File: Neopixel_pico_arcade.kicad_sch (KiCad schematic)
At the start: 10 parts

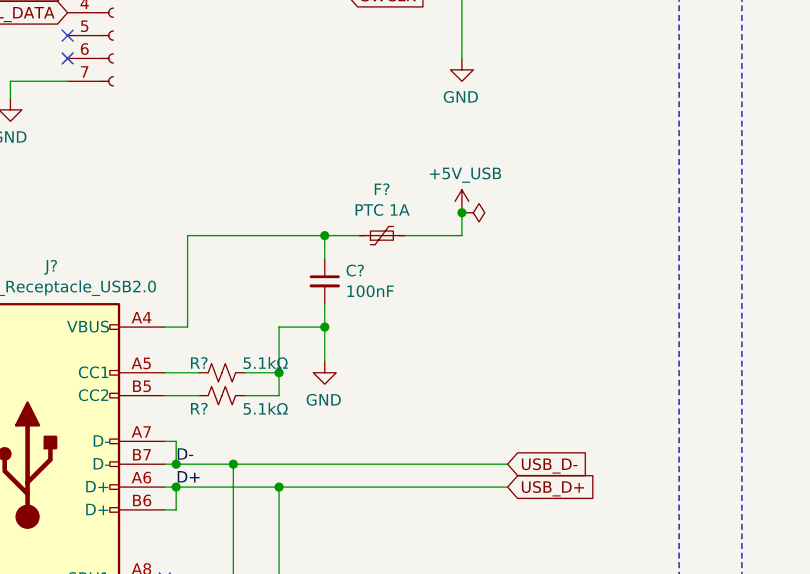
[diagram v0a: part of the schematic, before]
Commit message: Adds bulk capacitance for USB power
USB devices should be limited to at most 10µF capacitance to keep inrush
current under the specified limits.
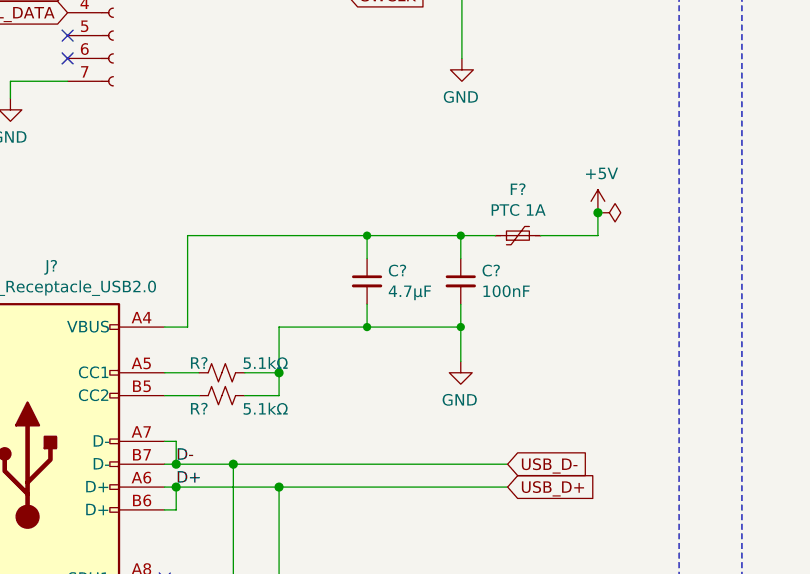
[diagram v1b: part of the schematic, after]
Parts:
- added C?: 4.7µF, Capacitor_SMD:C_0805_2012Metric_Pad1.18x1.45mm_HandSolder, symbol Device:C_Small
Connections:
- net GND: now also C?.2
- net at C?.1, F?.1, J?.A4 (VBUS)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: now also C?.1
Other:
- moved on the sheet: C?, F?
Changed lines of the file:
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@@
   (junction (at 69.215 90.17) (diameter 1.016) (color 0 0 0 0))
   (junction (at 69.215 102.87) (diameter 1.016) (color 0 0 0 0))
-  (junction (at 74.295 74.93) (diameter 1.016) (color 0 0 0 0))
-  (junction (at 74.295 85.09) (diameter 1.016) (color 0 0 0 0))
-  (junction (at 89.535 72.39) (diameter 1.016) (color 0 0 0 0))
+  (junction (at 78.994 74.93) (diameter 0) (color 0 0 0 0))
+  (junction (at 78.994 85.09) (diameter 0) (color 0 0 0 0))
+  (junction (at 89.408 74.93) (diameter 0) (color 0 0 0 0))
+  (junction (at 89.408 85.09) (diameter 0) (color 0 0 0 0))
+  (junction (at 104.648 72.39) (diameter 1.016) (color 0 0 0 0))
   (no_connect (at 45.72 52.705))
   (no_connect (at 45.72 55.245))
@@
     (stroke (width 0) (type solid) (color 0 0 0 0))
   )
-  (wire (pts (xy 59.055 74.93) (xy 74.295 74.93))
-    (stroke (width 0) (type solid) (color 0 0 0 0))
+  (wire (pts (xy 59.055 74.93) (xy 78.994 74.93))
+    (stroke (width 0) (type default) (color 0 0 0 0))
   )
   (wire (pts (xy 64.135 100.33) (xy 64.135 121.92))
@@
     (stroke (width 0) (type solid) (color 0 0 0 0))
   )
-  (wire (pts (xy 69.215 85.09) (xy 74.295 85.09))
+  (wire (pts (xy 69.215 85.09) (xy 78.994 85.09))
     (stroke (width 0) (type solid) (color 0 0 0 0))
   )
@@
     (stroke (width 0) (type solid) (color 0 0 0 0))
   )
-  (wire (pts (xy 74.295 74.93) (xy 74.295 77.47))
-    (stroke (width 0) (type solid) (color 0 0 0 0))
-  )
-  (wire (pts (xy 74.295 74.93) (xy 78.105 74.93))
-    (stroke (width 0) (type solid) (color 0 0 0 0))
-  )
-  (wire (pts (xy 74.295 82.55) (xy 74.295 85.09))
-    (stroke (width 0) (type solid) (color 0 0 0 0))
-  )
-  (wire (pts (xy 74.295 85.09) (xy 74.295 88.9))
-    (stroke (width 0) (type solid) (color 0 0 0 0))
-  )
   (wire (pts (xy 76.835 45.72) (xy 89.535 45.72))
     (stroke (width 0) (type solid) (color 0 0 0 0))
@@
     (stroke (width 0) (type solid) (color 0 0 0 0))
   )
+  (wire (pts (xy 78.994 74.93) (xy 78.994 77.47))
+    (stroke (width 0) (type default) (color 0 0 0 0))
+  )
+  (wire (pts (xy 78.994 74.93) (xy 89.408 74.93))
+    (stroke (width 0) (type default) (color 0 0 0 0))
+  )
+  (wire (pts (xy 78.994 82.55) (xy 78.994 85.09))
+    (stroke (width 0) (type default) (color 0 0 0 0))
+  )
+  (wire (pts (xy 78.994 85.09) (xy 89.408 85.09))
+    (stroke (width 0) (type solid) (color 0 0 0 0))
+  )
   (wire (pts (xy 79.375 134.62) (xy 83.185 134.62))
     (stroke (width 0) (type solid) (color 0 0 0 0))
   )
-  (wire (pts (xy 83.185 74.93) (xy 89.535 74.93))
-    (stroke (width 0) (type solid) (color 0 0 0 0))
-  )
   (wire (pts (xy 83.185 133.35) (xy 83.185 134.62))
     (stroke (width 0) (type solid) (color 0 0 0 0))
   )
+  (wire (pts (xy 89.408 74.93) (xy 89.408 77.47))
+    (stroke (width 0) (type solid) (color 0 0 0 0))
+  )
+  (wire (pts (xy 89.408 74.93) (xy 93.218 74.93))
+    (stroke (width 0) (type solid) (color 0 0 0 0))
+  )
+  (wire (pts (xy 89.408 82.55) (xy 89.408 85.09))
+    (stroke (width 0) (type solid) (color 0 0 0 0))
+  )
+  (wire (pts (xy 89.408 85.09) (xy 89.408 88.9))
+    (stroke (width 0) (type solid) (color 0 0 0 0))
+  )
   (wire (pts (xy 89.535 45.72) (xy 89.535 55.245))
     (stroke (width 0) (type solid) (color 0 0 0 0))
   )
-  (wire (pts (xy 89.535 74.93) (xy 89.535 72.39))
+  (wire (pts (xy 98.298 74.93) (xy 104.648 74.93))
+    (stroke (width 0) (type solid) (color 0 0 0 0))
+  )
+  (wire (pts (xy 104.648 74.93) (xy 104.648 72.39))
     (stroke (width 0) (type solid) (color 0 0 0 0))
   )
@@
     (pin "1")
   )
-  (symbol (lib_id "Generative_picture:+5V_USB") (at 89.535 72.39 0) (unit 1)
-    (in_bom yes) (on_board yes)
-    (property "Reference" "#PWR?" (id 0) (at 89.535 76.2 0)
-      (effects (font (size 1.27 1.27)) hide)
-    )
-    (property "Value" "+5V_USB" (id 1) (at 89.9033 68.0656 0))
-    (property "Footprint" "" (id 2) (at 89.535 72.39 0)
-      (effects (font (size 1.27 1.27)) hide)
-    )
-    (property "Datasheet" "" (id 3) (at 89.535 72.39 0)
+  (symbol (lib_id "Generative_picture:+5V_USB") (at 104.648 72.39 0) (unit 1)
+    (in_bom yes) (on_board yes)
+    (property "Reference" "#PWR?" (id 0) (at 104.648 76.2 0)
+      (effects (font (size 1.27 1.27)) hide)
+    )
+    (property "Value" "+5V" (id 1) (at 105.0163 68.0656 0))
+    (property "Footprint" "" (id 2) (at 104.648 72.39 0)
+      (effects (font (size 1.27 1.27)) hide)
+    )
+    (property "Datasheet" "" (id 3) (at 104.648 72.39 0)
       (effects (font (size 1.27 1.27)) hide)
     )
@@
     (pin "1")
   )
-  (symbol (lib_id "power:PWR_FLAG") (at 89.535 72.39 270) (unit 1)
-    (in_bom yes) (on_board yes)
-    (property "Reference" "#FLG?" (id 0) (at 91.44 72.39 0)
-      (effects (font (size 1.27 1.27)) hide)
-    )
-    (property "Value" "PWR_FLAG" (id 1) (at 92.71 72.39 90)
+  (symbol (lib_id "power:PWR_FLAG") (at 104.648 72.39 270) (unit 1)
+    (in_bom yes) (on_board yes)
+    (property "Reference" "#FLG?" (id 0) (at 106.553 72.39 0)
+      (effects (font (size 1.27 1.27)) hide)
+    )
+    (property "Value" "PWR_FLAG" (id 1) (at 107.823 72.39 90)
       (effects (font (size 1.27 1.27)) (justify left) hide)
     )
-    (property "Footprint" "" (id 2) (at 89.535 72.39 0)
-      (effects (font (size 1.27 1.27)) hide)
-    )
-    (property "Datasheet" "~" (id 3) (at 89.535 72.39 0)
+    (property "Footprint" "" (id 2) (at 104.648 72.39 0)
+      (effects (font (size 1.27 1.27)) hide)
+    )
+    (property "Datasheet" "~" (id 3) (at 104.648 72.39 0)
       (effects (font (size 1.27 1.27)) hide)
     )
@@
     (pin "1")
   )
-  (symbol (lib_id "power:GND") (at 74.295 88.9 0) (mirror y) (unit 1)
-    (in_bom yes) (on_board yes)
-    (property "Reference" "#PWR?" (id 0) (at 74.295 95.25 0)
-      (effects (font (size 1.27 1.27)) hide)
-    )
-    (property "Value" "GND" (id 1) (at 74.1807 93.2244 0))
-    (property "Footprint" "" (id 2) (at 74.295 88.9 0)
-      (effects (font (size 1.27 1.27)) hide)
-    )
-    (property "Datasheet" "" (id 3) (at 74.295 88.9 0)
+  (symbol (lib_id "power:GND") (at 89.408 88.9 0) (mirror y) (unit 1)
+    (in_bom yes) (on_board yes)
+    (property "Reference" "#PWR?" (id 0) (at 89.408 95.25 0)
+      (effects (font (size 1.27 1.27)) hide)
+    )
+    (property "Value" "GND" (id 1) (at 89.2937 93.2244 0))
+    (property "Footprint" "" (id 2) (at 89.408 88.9 0)
+      (effects (font (size 1.27 1.27)) hide)
+    )
+    (property "Datasheet" "" (id 3) (at 89.408 88.9 0)
       (effects (font (size 1.27 1.27)) hide)
     )
@@
     (pin "2")
   )
-  (symbol (lib_id "Device:Polyfuse_Small") (at 80.645 74.93 90) (unit 1)
-    (in_bom yes) (on_board yes)
-    (property "Reference" "F?" (id 0) (at 80.645 69.8308 90))
-    (property "Value" "PTC 1A" (id 1) (at 80.645 72.13 90))
-    (property "Footprint" "Generative_picture:Belfuse_0ZCJ" (id 2) (at 85.725 73.66 0)
+  (symbol (lib_id "Device:Polyfuse_Small") (at 95.758 74.93 90) (unit 1)
+    (in_bom yes) (on_board yes)
+    (property "Reference" "F?" (id 0) (at 95.758 69.8308 90))
+    (property "Value" "PTC 1A" (id 1) (at 95.758 72.13 90))
+    (property "Footprint" "Generative_picture:Belfuse_0ZCJ" (id 2) (at 100.838 73.66 0)
       (effects (font (size 1.27 1.27)) (justify left) hide)
     )
-    (property "Datasheet" "~" (id 3) (at 80.645 74.93 0)
+    (property "Datasheet" "~" (id 3) (at 95.758 74.93 0)
       (effects (font (size 1.27 1.27)) hide)
     )
@@
     (pin "2")
   )
-  (symbol (lib_id "Device:C_Small") (at 74.295 80.01 0) (unit 1)
-    (in_bom yes) (on_board yes)
-    (property "Reference" "C?" (id 0) (at 76.6192 78.8606 0)
+  (symbol (lib_id "Device:C_Small") (at 78.994 80.01 0) (unit 1)
+    (in_bom yes) (on_board yes)
+    (property "Reference" "C?" (id 0) (at 81.3182 78.8606 0)
       (effects (font (size 1.27 1.27)) (justify left))
     )
-    (property "Value" "100nF" (id 1) (at 76.619 81.159 0)
+    (property "Value" "4.7µF" (id 1) (at 81.318 81.159 0)
       (effects (font (size 1.27 1.27)) (justify left))
     )
-    (property "Footprint" "Capacitor_SMD:C_0805_2012Metric_Pad1.18x1.45mm_HandSolder" (id 2) (at 74.295 80.01 0)
-      (effects (font (size 1.27 1.27)) hide)
-    )
-    (property "Datasheet" "~" (id 3) (at 74.295 80.01 0)
+    (property "Footprint" "Capacitor_SMD:C_0805_2012Metric_Pad1.18x1.45mm_HandSolder" (id 2) (at 78.994 80.01 0)
+      (effects (font (size 1.27 1.27)) hide)
+    )
+    (property "Datasheet" "~" (id 3) (at 78.994 80.01 0)
+      (effects (font (size 1.27 1.27)) hide)
+    )
+    (pin "1")
+    (pin "2")
+  )
+  (symbol (lib_id "Device:C_Small") (at 89.408 80.01 0) (unit 1)
+    (in_bom yes) (on_board yes)
+    (property "Reference" "C?" (id 0) (at 91.7322 78.8606 0)
+      (effects (font (size 1.27 1.27)) (justify left))
+    )
+    (property "Value" "100nF" (id 1) (at 91.732 81.159 0)
+      (effects (font (size 1.27 1.27)) (justify left))
+    )
+    (property "Footprint" "Capacitor_SMD:C_0805_2012Metric_Pad1.18x1.45mm_HandSolder" (id 2) (at 89.408 80.01 0)
+      (effects (font (size 1.27 1.27)) hide)
+    )
+    (property "Datasheet" "~" (id 3) (at 89.408 80.01 0)
       (effects (font (size 1.27 1.27)) hide)
     )
@@
     )
     (path "/4f1fe51c-79e1-410a-ae57-948c663e40fc"
-      (reference "#PWR?") (unit 1) (value "+5V_USB") (footprint "")
+      (reference "#PWR?") (unit 1) (value "+5V") (footprint "")
     )
     (path "/ed4fcb8f-53b7-458f-bfaa-4aa127051293/5012d051-6b17-499c-a0aa-a1866e5f78d5"
@@
       (reference "C?") (unit 1) (value "100nF") (footprint "Capacitor_SMD:C_0805_2012Metric_Pad1.15x1.40mm_HandSolder")
     )
+    (path "/3dcd957e-2bc0-456f-b0ec-92b7bc5b3d89"
+      (reference "C?") (unit 1) (value "4.7µF") (footprint "Capacitor_SMD:C_0805_2012Metric_Pad1.18x1.45mm_HandSolder")
+    )
     (path "/ed4fcb8f-53b7-458f-bfaa-4aa127051293/45a55838-3e5c-4754-93c1-b22db5fcfdfc"

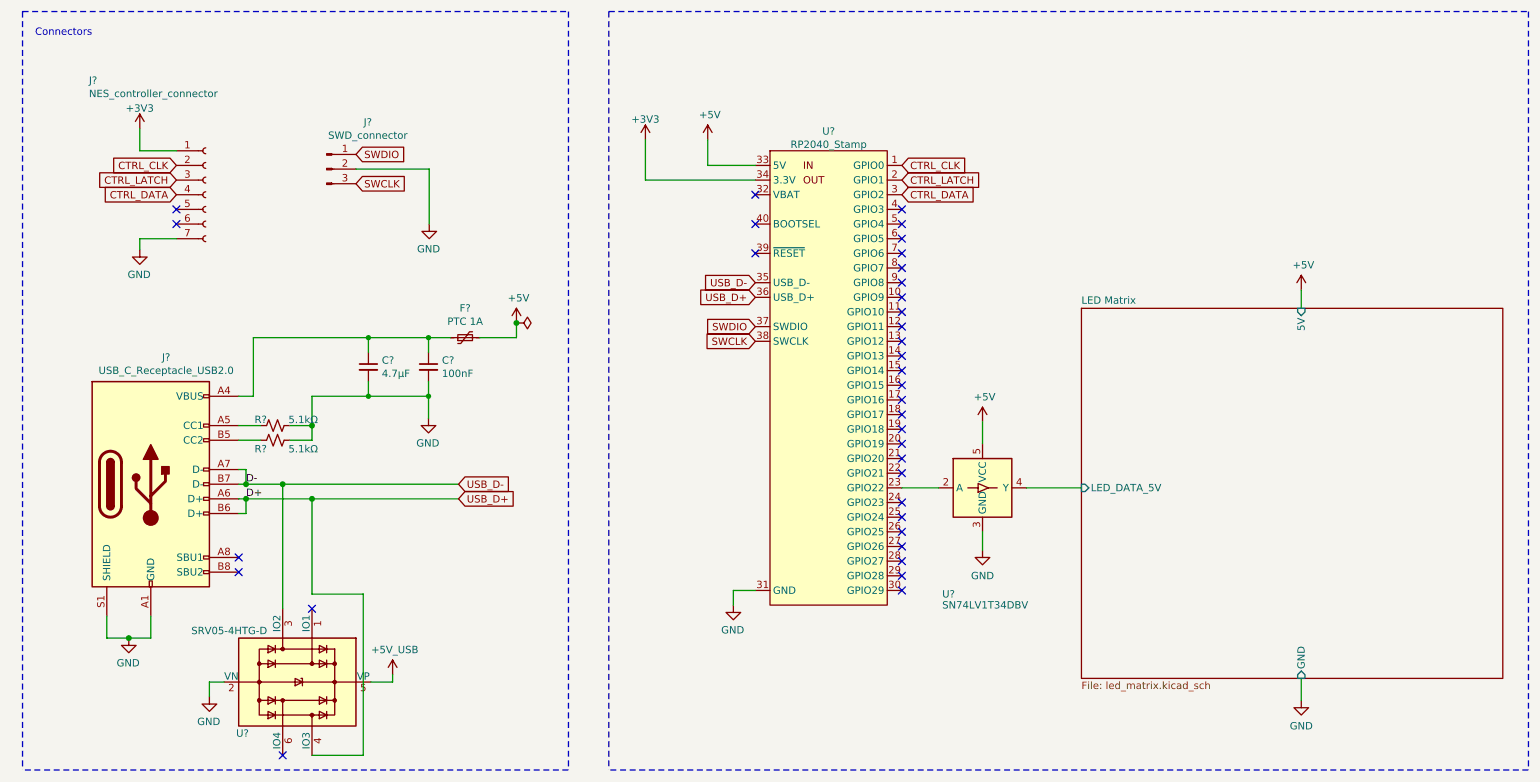
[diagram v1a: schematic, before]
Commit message: Adds jumpers to latch and clock lines to make rework easier
I've switched those two pins a few times already during prototyping.
With the normally closed jumpers it will be easier to swap them if I
make a mistake while laying out the board.
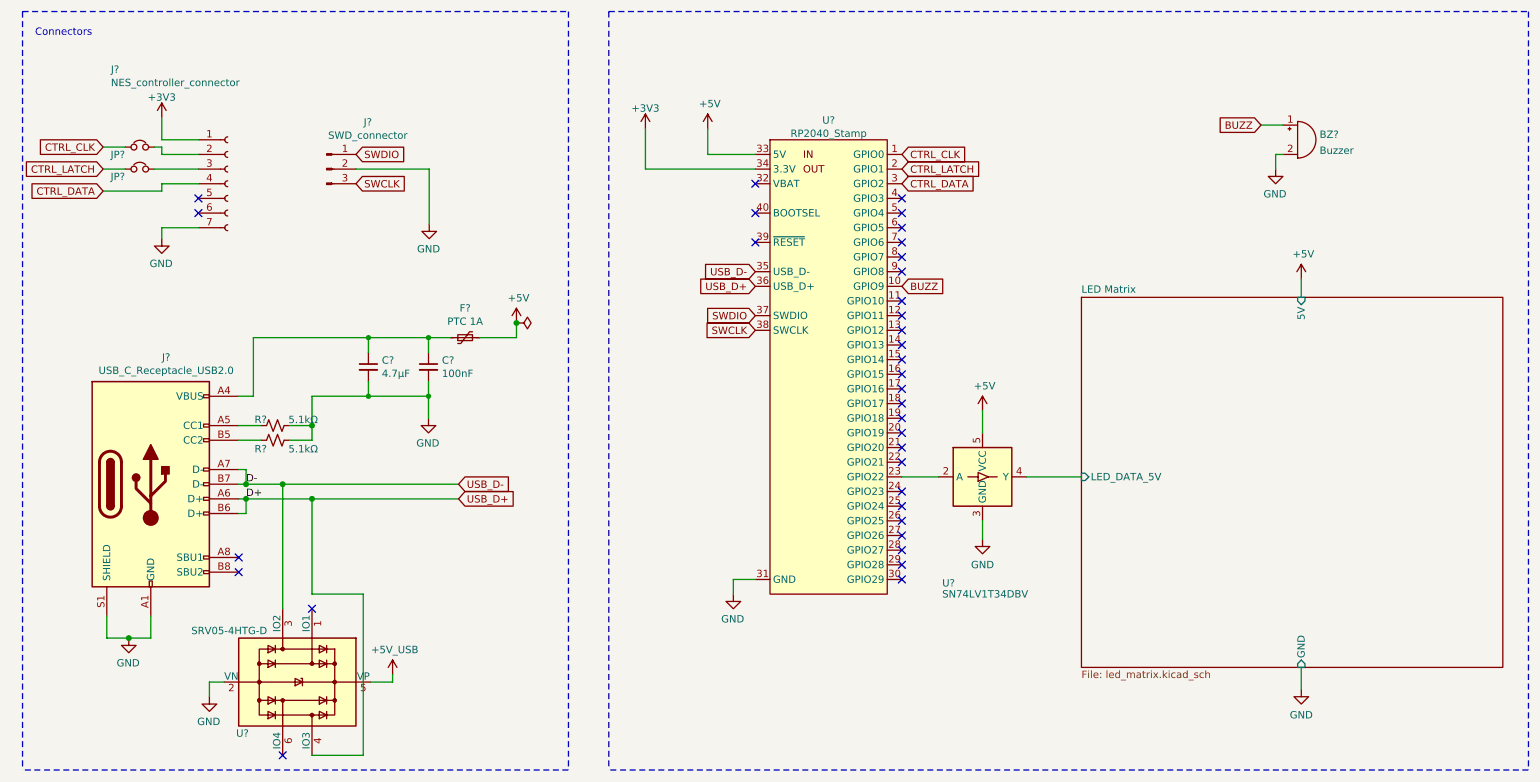
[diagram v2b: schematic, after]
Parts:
- added BZ?: Buzzer, symbol Device:Buzzer
- added JP? (x2): jmp, symbol Device:Jumper_NC_Small
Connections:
- net CTRL_CLK: now also JP?.1; no longer J?.2 (Pin_2)
- net CTRL_LATCH: now also JP?.1; no longer J?.3 (Pin_3)
- net GND: now also BZ?.2 (+)
- net BUZZ: now reaches U?.10 (GPIO9)
- net BUZZ: now also BZ?.1 (-)
- new net: J?.2 (Pin_2), JP?.2
- new net: J?.3 (Pin_3), JP?.2
- no-connect marks 35 -> 34
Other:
- moved on the sheet: J?, U?
